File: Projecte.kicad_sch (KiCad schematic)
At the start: 42 parts, among them Q1 IRLZ34N, Q2 BC107, Q3 IRLZ34N, Q4 IRLZ34N, Q5 IRLZ34N, Q6 IRLZ34N, U1 PIC18F448-IP, U2 LM358, U3 R-786.5-0.5, U4 MCP2551-I-P, U5 AMS1117-3.3, U6 TXB0108PW, U7 LM7805_TO220, Y1 Crystal

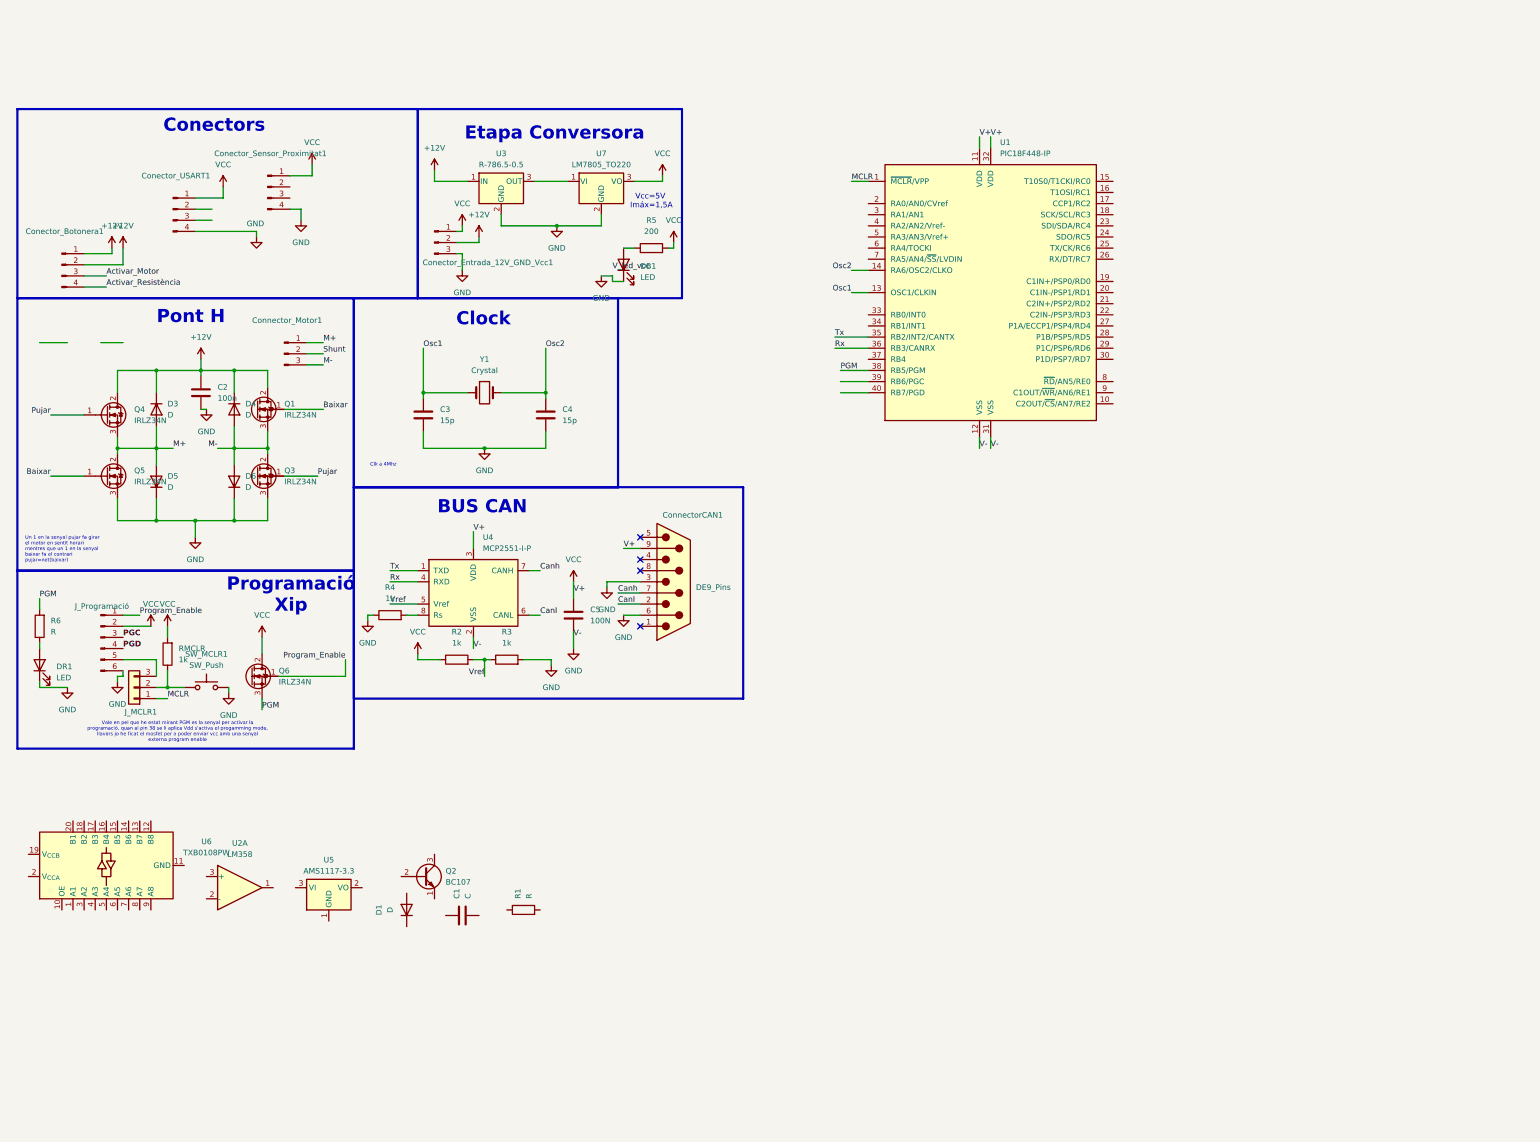
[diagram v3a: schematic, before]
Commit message: V2
S'ha afeguit el relé, s'han conectat els senyals de control al micro, s'han corregit errors i s'ha dinamitzat el esquematic.
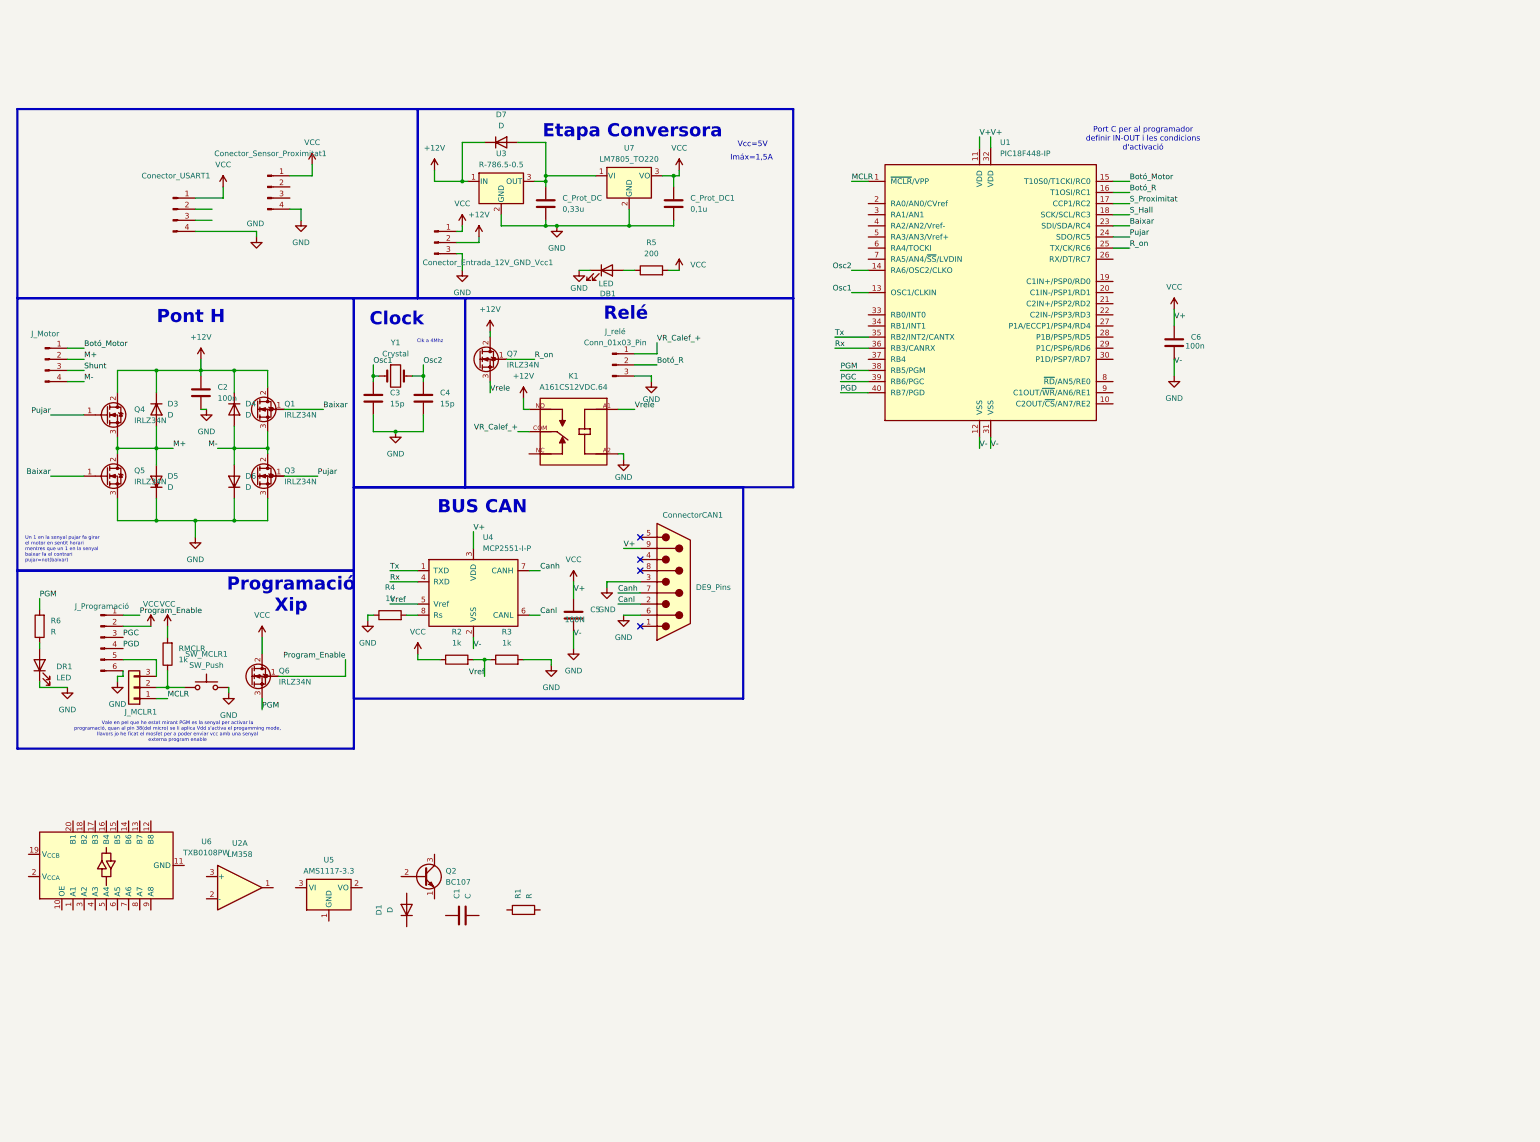
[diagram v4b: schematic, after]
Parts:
- removed Conector_Botonera1: Conn_01x04_Pin, symbol Connector:Conn_01x04_Pin
- removed Connector_Motor1: Conn_01x03_Pin, symbol Connector:Conn_01x03_Pin
- added C6: 100n, symbol Device:C
- added C_Prot_DC: 0,33u, symbol Device:C
- added C_Prot_DC1: 0,1u, symbol Device:C
- added D7: D, symbol Device:D
- added J_Motor: Conn_01x04_Pin, symbol Connector:Conn_01x04_Pin
- added J_relé: Conn_01x03_Pin, symbol Connector:Conn_01x03_Pin
- added K1: A161CS12VDC.64, A161CS12VDC.64:RELAY_A161CS12VDC.64, symbol Usuari:A161CS12VDC.64
- added Q7: IRLZ34N, Package_TO_SOT_THT:TO-220-3_Vertical, symbol Transistor_FET:IRLZ34N
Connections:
- net +12V: now also D7.1 (K), K1.NO, Q7.2 (D)
- net Baixar: now also U1.23 (SDI/SDA/RC4)
- net GND: now also C6.2, C_Prot_DC.2, C_Prot_DC1.2, J_relé.3 (Pin_3), K1.A2
- net M+: now also J_Motor.2 (Pin_2)
- net M-: now also J_Motor.4 (Pin_4)
- net PGC: now also U1.39 (RB6/PGC)
- net PGD: now also U1.40 (RB7/PGD)
- net Pujar: now also U1.24 (SDO/RC5)
- net Shunt: now also J_Motor.3 (Pin_3)
- net VCC: now also C6.1, C_Prot_DC1.1
- net Botó_Motor: now reaches U1.15 (T10S0/T1CKI/RC0)
- net Botó_Motor: now also J_Motor.1 (Pin_1)
- net Botó_R: now reaches U1.16 (T1OSI/RC1)
- net Botó_R: now also J_relé.2 (Pin_2)
- net S_Proximitat: now reaches U1.17 (CCP1/RC2)
- net S_Hall: now reaches U1.18 (SCK/SCL/RC3)
- net R_on: now reaches U1.25 (TX/CK/RC6)
- net R_on: now also Q7.1 (G)
- net at U3.3 (OUT), U7.1 (VI): now also C_Prot_DC.1, D7.2 (A)
- new net VR_Calef_+: J_relé.1 (Pin_1), K1.COM
- new net Vrele: K1.A1, Q7.3 (S)
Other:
- note added: "Port C per al programador definir IN-OUT i les condicions d'activació"
- note added: "Relé"
- note added: "Vale en pel que he estat mirant PGM es la senyal per activar la programació, quan al pin 38(del micro) se li aplica Vdd s'activa el progamming mode, llavors jo he ficat el mosfet per a poder enviar vcc amb una senyal externa program enable"
- note removed: "Conectors"
- note removed: "Vale en pel que he estat mirant PGM es la senyal per activar la programació, quan al pin 38 se li aplica Vdd s'activa el progamming mode, llavors jo he ficat el mosfet per a poder enviar vcc amb una senyal externa program enable"
- moved on the sheet: C3, C4, DB1, R5, U7, Y1

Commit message: Update Proyecto.kicad_sch
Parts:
- removed C1: C, symbol Device:C
- removed Conector_Sensor_Proximitat1, J_Motor: Conn_01x04_Pin, symbol Connector:Conn_01x04_Pin
- removed D1: D, symbol Device:D
- removed Q2: BC107, Package_TO_SOT_THT:TO-18-3, symbol Transistor_BJT:BC107
- removed R1: R, symbol Device:R
- added J1, J2: Conn_01x04_Pin, symbol Connector:Conn_01x04_Pin
- added R10, R9: 10k, symbol Device:R
- added R11: 0, symbol Device:R
- added R7: 6k2, symbol Device:R
- added R8: 1k, symbol Device:R
- added R_shunt1: 0.005, symbol Device:R
- added U8: MMC5883MA, Package_LGA:LGA-16_3x3mm_P0.5mm, symbol Sensor_Magnetic:MMC5883MA
- renumbered C_Prot_DC to C_Prot_DC2, J_Programació to J_Programaci1, J_relé to J_rel1, RMCLR to RMCLR1
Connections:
- net S_Hall is gone; now on net SCL: U1.18 (SCK/SCL/RC3)
- net +12V: now also J1.1 (Pin_1)
- net Baixar: now also U1.4 (RA2/AN2/Vref-); no longer U1.23 (SDI/SDA/RC4)
- net Canh: no longer ConnectorCAN1.7, U4.7 (CANH)
- net Canl: no longer ConnectorCAN1.2, U4.6 (CANL)
- net GND: now also U6.11 (GND), J2.4 (Pin_4), R11.2, U8.10 (CAP), U8.11 (GND), U8.9 (GND); no longer C_Prot_DC1.2, C_Prot_DC2.2, Conector_Entrada_12V_GND_Vcc1.3 (Pin_3), D5.1 (K), D6.1 (K), J_rel1.3 (Pin_3), K1.A2, Q3.3 (S), Q5.3 (S), U3.2 (GND), U7.2 (GND)
- net M+: now also J1.2 (Pin_2)
- net M-: now also J1.3 (Pin_3)
- net Pujar: now also U1.5 (RA3/AN3/Vref+); no longer U1.24 (SDO/RC5)
- net R_on: now also U1.33 (RB0/INT0), R7.2; no longer Q7.1 (G), U1.25 (TX/CK/RC6)
- net Rx: no longer U1.36 (RB3/CANRX), U4.4 (RXD)
- net Tx: no longer U1.35 (RB2/INT2/CANTX), U4.1 (TXD)
- net GNDPWR: now reaches U5.1 (GND)
- net GNDPWR: now also C_Prot_DC1.2, C_Prot_DC2.2, Conector_Entrada_12V_GND_Vcc1.3 (Pin_3), D5.1 (K), D6.1 (K), J_rel1.3 (Pin_3), K1.A2, Q3.3 (S), Q5.3 (S), U2.2 (-), U3.2 (GND), U7.2 (GND), R11.1, R8.2, R_shunt1.2
- net Vcc_3.3V: now reaches U5.2 (VO)
- net Vcc_3.3V: now also U6.2 (V_{CCA}), U8.13 (VDDIO), U8.2 (VDD)
- net Vcc: now reaches U5.3 (VI)
- net Vcc: now also U6.10 (OE), U6.19 (V_{CCB})
- net CORRENT!: now reaches U1.2 (RA0/AN0/CVref)
- net CORRENT!: now also U2.1
- net S_entrada: now reaches U1.20 (C1IN-/PSP1/RD1)
- net S_entrada: now also J2.2 (Pin_2)
- net S_sortida: now reaches U1.21 (C2IN+/PSP2/RD2)
- net S_sortida: now also J2.3 (Pin_3)
- net shunt: now reaches U2.3 (+)
- net shunt: now also J1.4 (Pin_4), R_shunt1.1
- net SCL: now reaches U6.1 (A1)
- net SCL_S: now reaches U6.20 (B1)
- net SCL_S: now also U8.1 (SCL)
- net Botó_Motor renamed Boto_Motor
- net Botó_R renamed Boto_R
- net S_Proximitat: no longer names the net of U1.17 (CCP1/RC2)
- new net: Q7.1 (G), R7.1, R8.1
- new net SDA: U1.23 (SDI/SDA/RC4)
- no-connect marks 4 -> 28
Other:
- note added: "27/03/2025"
- note added: "Adaptador de nivell lògic per bus i2c del micro al sensor hall"
- note added: "Bus Usart"
- note added: "CORRENT! és el shunt avisant de que hi ha un obstacle en el camí"
- note added: "Jordi Comas, Elena Sans"
- note added: "MALETER"
- note added: "Microcontrolador"
- note added: "Regulador de tensió de 5V a 3.3V"
- note added: "Resistència Calefactable"
- note added: "Sensor Hall"
- note added: "Sensor proximitat"
- note added: "Shunt"
- note added: "apagar? es refereix a si el motor ha de parar pel final de carrera"
- note added: "juntem gnds els de potència i els digitals"
- moved on the sheet: C6, Conector_USART1, DB1, J_MCLR1, J_Programaci1, J_rel1, K1, Q7, R5, RMCLR1, SW_MCLR1, U2A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

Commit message: Update Proyecto.kicad_sch
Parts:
- added C1: 100n, symbol Device:C
- J1: value Conn_01x04_Pin -> Conn_motor
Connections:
- net +12V: now also C1.1
- net Canh: now also ConnectorCAN1.7, U4.7 (CANH)
- net Canl: now also ConnectorCAN1.2, U4.6 (CANL)
- net Datos_i2c: now also U1.19 (C1IN+/PSP0/RD0)
- net GNDPWR: now also D5.2 (A), D6.2 (A), C1.2; no longer D5.1 (K), D6.1 (K)
- net M+: now also D5.1 (K); no longer D5.2 (A)
- net M-: now also D6.1 (K); no longer D6.2 (A)
- net Rx: now also U1.36 (RB3/CANRX), U4.4 (RXD)
- net SDA: now also U6.3 (A2)
- net Tx: now also U1.35 (RB2/INT2/CANTX), U4.1 (TXD)
- net Vcc: now also R10.1
- net Vcc_3.3V: now also R9.1
- net apagar?: now also R10.2, U1.34 (RB1/INT1), U6.13 (B7)
- net final_carrera: now also R9.2, U6.8 (A7), U8.15 (INT)
- net i2c_nivellat: now also U6.18 (B2), U8.16 (SDA)
- net usart_rx: now also U1.26 (RX/DT/RC7)
- net usart_tx: now also U1.25 (TX/CK/RC6)
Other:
- note added: "sortida_motor"
- moved on the sheet: Conector_Entrada_12V_GND_Vcc1, D5, D6, J1

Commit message: Sch_Post_Show
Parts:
- removed C2: 100n, symbol Device:C
- removed J1: Conn_motor, symbol Connector:Conn_01x04_Pin
- removed J_Programaci1: Conn_01x06_Pin, symbol Connector:Conn_01x06_Pin
- removed Q6: IRLZ34N, Package_TO_SOT_THT:TO-220-3_Vertical, symbol Transistor_FET:IRLZ34N
- removed R7: 6k2, symbol Device:R
- added C7: 100n, symbol Device:C
- added D8: D, symbol Device:D
- added J_Programació: Conn_01x05_Pin, symbol Connector:Conn_01x05_Pin
- added J_mOTOR: Conn_01x02_Pin, symbol Connector:Conn_01x02_Pin
- added R12: 120R, symbol Device:R
- renumbered J2 to J_Sensor_Prox
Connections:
- net Canh: now also R12.2
- net Canl: now also R12.1
- net GND: now also C_Prot_DC1.2, C_Prot_DC2.2, U7.2 (GND), C7.2, J_Programació.5 (Pin_5); no longer ConnectorCAN1.3, ConnectorCAN1.6
- net GNDPWR: now also K1.NC, D8.2 (A); no longer C_Prot_DC1.2, C_Prot_DC2.2, D5.2 (A), D6.2 (A), Q3.3 (S), Q5.3 (S), R8.2, U7.2 (GND)
- net M+: now also J_mOTOR.1 (Pin_1)
- net M-: now also J_mOTOR.2 (Pin_2)
- net PGC: now also J_Programació.2 (Pin_2)
- net PGD: now also J_Programació.3 (Pin_3)
- net R_on: now also Q7.1 (G), R8.1
- net VCC: now also J_Sensor_Prox.1 (Pin_1), C7.1, J_Programació.1 (Pin_1); no longer ConnectorCAN1.9
- net Vrele: now also D8.1 (K)
- net shunt: now also D5.2 (A), D6.2 (A), Q3.3 (S), Q5.3 (S)
- net Vpp: now reaches J_MCLR1.3 (Pin_3)
- net Vpp: now also J_Programació.4 (Pin_4)
- no-connect marks 28 -> 31
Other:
- note added: "ALIMENTACIÓ"
- note added: "CANVIAR"
- note added: "CANVIAR a open drain bidi 1 bit"
- note added: "Relé_Resistencia"
- note removed: "Etapa Conversora"
- note removed: "Relé"
- note removed: "Resistència Calefactable"
- note removed: "Vale en pel que he estat mirant PGM es la senyal per activar la programació, quan al pin 38(del micro) se li aplica Vdd s'activa el progamming mode, llavors jo he ficat el mosfet per a poder enviar vcc amb una senyal externa program enable"
- moved on the sheet: C1, C3, C4, C5, C6, C_Prot_DC1, C_Prot_DC2, Conector_Entrada_12V_GND_Vcc1, Conector_USART1, ConnectorCAN1, D3, D4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

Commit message: Primer_Layout
S'han aplicat le footprints als components i s'ha fet un primer placement a la placa de manera que els components de una mateixa etapa quedin junts.
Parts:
- removed Conector_Entrada_12V_GND_Vcc1: Conn_01x03_Pin, symbol Connector:Conn_01x03_Pin
- added J_Alimentaci1: Conn_01x02_Pin, Connector_PinHeader_2.54mm:PinHeader_1x02_P2.54mm_Vertical, symbol Connector:Conn_01x02_Pin
- C1, C3, C4, C6, C7, C_Prot_DC1, C_Prot_DC2: footprint (none) -> Capacitor_SMD:C_0805_2012Metric
- C5: value 100N -> 100n; footprint (none) -> Capacitor_SMD:C_0805_2012Metric
- Conector_USART1: footprint (none) -> Connector_PinHeader_2.54mm:PinHeader_1x04_P2.54mm_Vertical
- D3, D4, D5, D6, D7, D8: footprint (none) -> Diode_THT:D_DO-41_SOD81_P10.16mm_Horizontal
- J_Programaci1: renamed from J_Programació; footprint (none) -> Connector_PinHeader_2.54mm:PinHeader_1x05_P2.54mm_Vertical
- J_Sensor_Prox1: renamed from J_Sensor_Prox; footprint (none) -> Connector_PinHeader_2.54mm:PinHeader_1x04_P2.54mm_Vertical
- J_mOTOR1: renamed from J_mOTOR; footprint (none) -> Connector_PinHeader_2.54mm:PinHeader_1x02_P2.54mm_Vertical
- J_res1: renamed from J_rel1; footprint (none) -> Connector_PinHeader_2.54mm:PinHeader_1x03_P2.54mm_Vertical
- K1: footprint A161CS12VDC.64:RELAY_A161CS12VDC.64 -> Library:RELAY_A161CS12VDC.64
- R10, R11, R12, R2, R3, R4, R8, R9, R_shunt1: footprint (none) -> Resistor_SMD:R_0805_2012Metric
- U2: footprint (none) -> Library:LM358
- Y1: footprint (none) -> Crystal:Crystal_SMD_HC49-SD
- renumbered DB1 to L_ON1, DR1 to L_PR1
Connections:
- net +12V: now also J_Alimentaci1.1 (Pin_1)
- net GNDPWR: now also J_Alimentaci1.2 (Pin_2)
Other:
- moved on the sheet: J_mOTOR1, J_res1
